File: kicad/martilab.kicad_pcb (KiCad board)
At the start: 2 copper layers, 98.8 x 60.5 mm, 11 parts, among them J1 Conn_01x20, J2 Conn_01x20, J3 Conn_01x02, Q2 BS250, SW1 SW_Push, U1 Pico, U2 DFR0299, U3 RTC DS1307

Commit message: add schema
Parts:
- Q2: value BS250 -> PMOS
- moved SW1 7.91 mm to (112.8, 53.0), turned to 0 degrees
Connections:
- SW1 pad 1: Net-(J1-Pin_2) -> GND
- SW1 pad 2: GND -> Net-(J1-Pin_2)

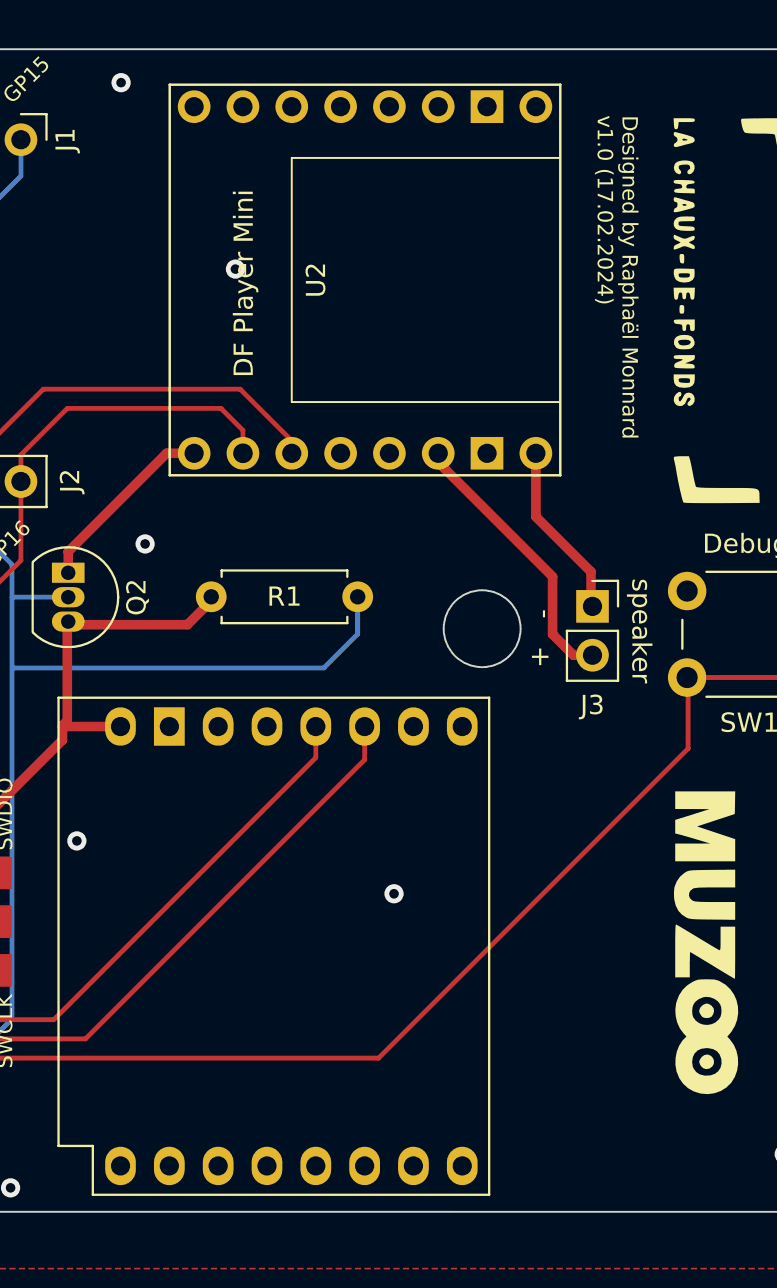
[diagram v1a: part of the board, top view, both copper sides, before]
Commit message: create v1.1 and add enclosure files
reduce file size

add git lfs
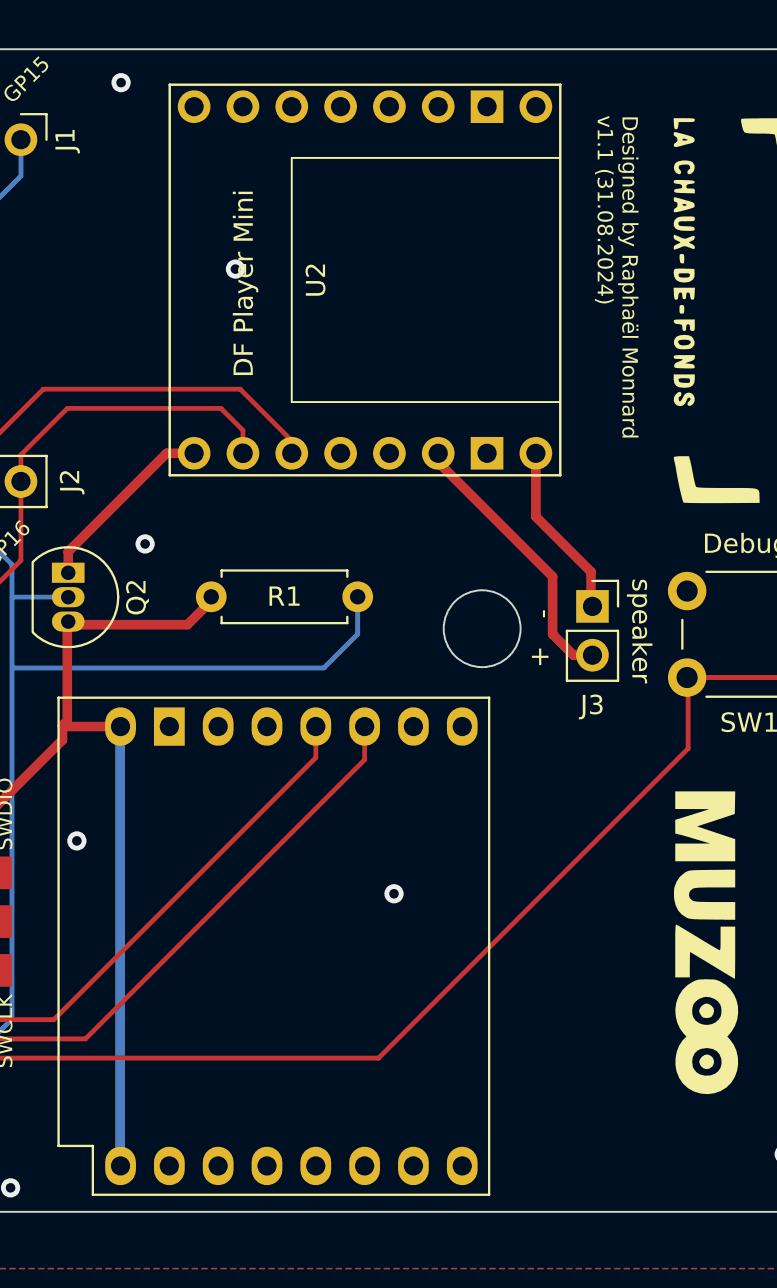
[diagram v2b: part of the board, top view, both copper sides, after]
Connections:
- U3 pad 8: unconnected-(U3-3V3-Pad8) -> Net-(J2-Pin_1)
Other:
- board text added: "Designed by Raphaël Monnard v1.1 (31.08.2024)"
- board text removed: "Designed by Raphaël Monnard v1.0 (17.02.2024)"
